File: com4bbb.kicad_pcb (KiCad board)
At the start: 4 copper layers, 54.6 x 86.4 mm, 67 parts, among them J101 RS485, J102 PWR, J103 DCF77, J104 PPS, J201 USB_B_Micro, J202 JTAG, P8 BeagleBone_Black_Header, P9 BeagleBone_Black_Header, SW101 Reset, SW102 PWR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

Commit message: Add PPS output
Signed-off-by: Benedikt Spranger <b.spranger@linutronix.de>
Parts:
- added J105: PPSOUT, Connector_PinHeader_2.54mm:PinHeader_1x02_P2.54mm_Vertical, F.Cu at (160.9, 108.1)
- added Q101: AO3400A, Package_TO_SOT_SMD:SOT-23, F.Cu at (159.9, 102.9)
- added R119: 100, Resistor_SMD:R_0402_1005Metric, F.Cu at (159.6, 99.4)
- added R120: 47k, Resistor_SMD:R_0402_1005Metric, F.Cu at (160.9, 99.4)
- added R121: 1k, Resistor_SMD:R_0402_1005Metric, F.Cu at (162.4, 102.6)
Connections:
- P9 pad 42: unconnected-(P9-Pin_42-Pad42) -> /PPS_OUT
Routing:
- net +5V: track 9.05 -> 75.3 mm, vias 0 -> 1
- net /PPS_OUT: track 0.00 -> 49.4 mm, vias 0 -> 2
- net Net-(J105-Pin_1): track 0.00 -> 7.00 mm
- net Net-(Q101-G): track 0.00 -> 3.32 mm

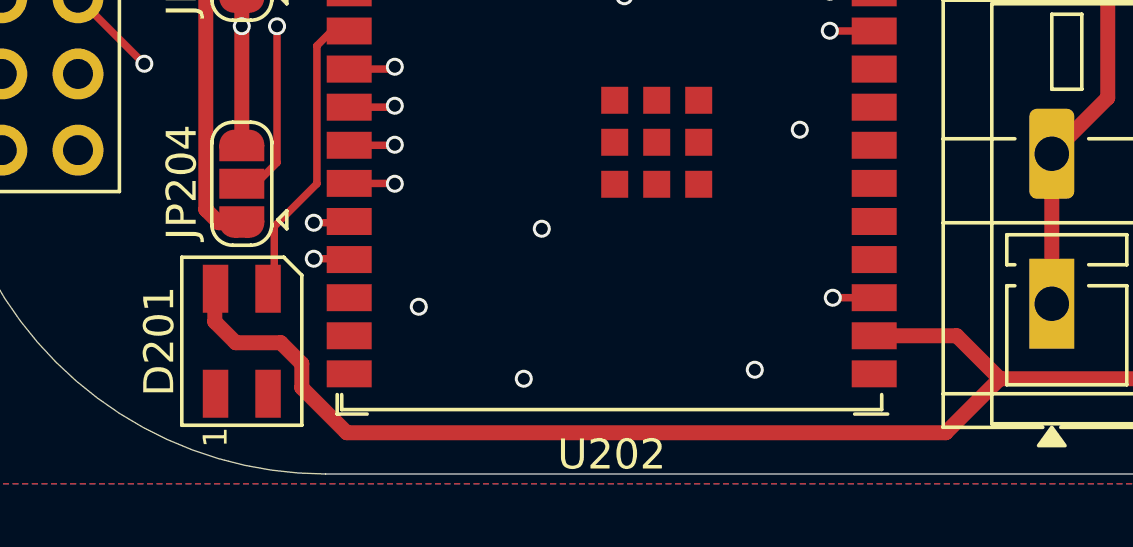
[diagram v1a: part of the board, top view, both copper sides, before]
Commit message: Fix SK6812 footprint mess
Signed-off-by: Benedikt Spranger <b.spranger@linutronix.de>
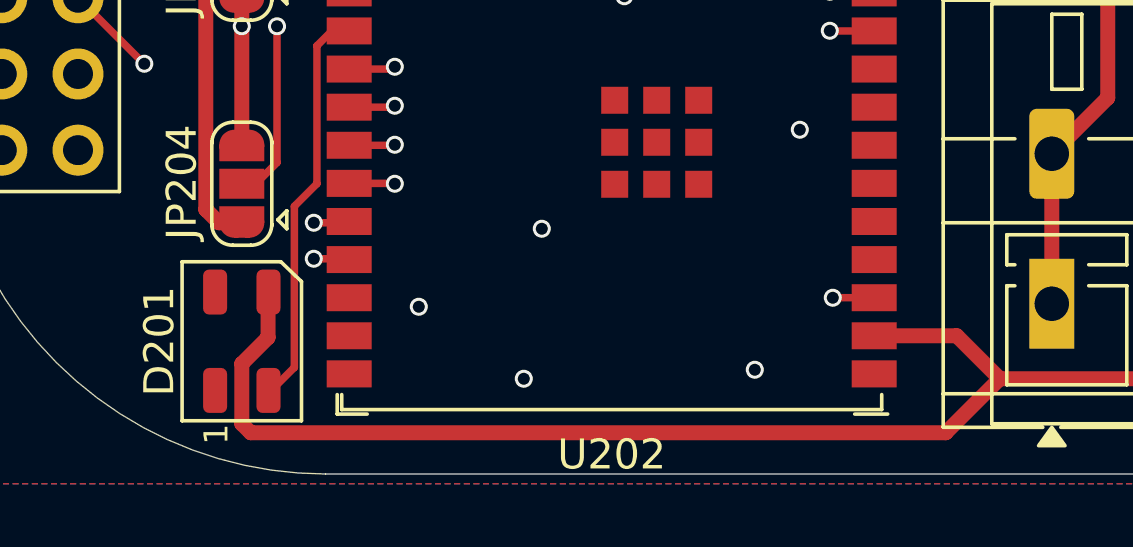
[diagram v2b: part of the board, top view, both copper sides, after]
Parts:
- D201: value SK6812MINI -> SK6812MINI-HS-012; footprint LED_SMD:LED_SK6812MINI_PLCC4_3.5x3.5mm_P1.75mm -> LED_SMD:LED_WS2812B-Mini_PLCC4_3.5x3.5mm
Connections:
- D201 pad 1: unconnected-(D201-DOUT-Pad1) -> GNDD
- D201 pad 2: GNDD -> Net-(D201-DIN)
- D201 pad 3: Net-(D201-DIN) -> +3V3
- D201 pad 4: +3V3 -> unconnected-(D201-DOUT-Pad4)
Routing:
- net Net-(D201-DIN): track 9.18 -> 13.0 mm
- net +3V3: track 222.5 -> 223.5 mm
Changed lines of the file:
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@@
 	(net 33 "Net-(D114-K)")
 	(net 34 "Net-(D114-A)")
-	(net 35 "unconnected-(D201-DOUT-Pad1)")
+	(net 35 "unconnected-(D201-DOUT-Pad4)")
 	(net 36 "Net-(D201-DIN)")
 	(net 37 "Net-(J201-Shield)")
@@
 		)
 	)
-	(footprint "LED_SMD:LED_SK6812MINI_PLCC4_3.5x3.5mm_P1.75mm"
+	(footprint "LED_SMD:LED_WS2812B-Mini_PLCC4_3.5x3.5mm"
 		(layer "F.Cu")
 		(at 124.3701 124.6324 90)
-		(descr "3.5mm x 3.5mm PLCC4 Addressable RGB LED NeoPixel, https://cdn-shop.adafruit.com/product-files/2686/SK6812MINI_REV.01-1-2.pdf")
-		(tags "LED RGB NeoPixel Mini PLCC-4 3535")
+		(descr "Addressable RGB LED NeoPixel Mini, 12 mA, https://web.archive.org/web/20200131233647/http://www.world-semi.com/DownLoadFile/112")
+		(tags "LED RGB NeoPixel Mini")
 		(property "Reference" "D201"
 			(at 0 -2.75 90)
@@
 			)
 		)
-		(property "Value" "SK6812MINI"
+		(property "Value" "SK6812MINI-HS-012"
 			(at 0 3.25 90)
 			(layer "F.Fab")
@@
 			)
 		)
-		(property "Datasheet" "https://cdn-shop.adafruit.com/product-files/2686/SK6812MINI_REV.01-1-2.pdf"
+		(property "Datasheet" "https://jlcpcb.com/api/file/downloadByFileSystemAccessId/8588920813789581312"
 			(at 0 0 90)
 			(unlocked yes)
@@
 			)
 		)
-		(property ki_fp_filters "LED*SK6812MINI*PLCC*3.5x3.5mm*P1.75mm*")
+		(property ki_fp_filters "LED*WS2812B-Mini*PLCC*3.5x3.5mm")
 		(sheetname "/ESP32/")
 		(sheetfile "esp32.kicad_sch")
 		(attr smd)
 		(fp_line
-			(start -2.8 -2)
-			(end 2.8 -2)
+			(start -2.65 -1.99)
+			(end 2.65 -1.99)
 			(stroke
 				(width 0.12)
@@
 		)
 		(fp_line
-			(start -2.8 -2)
-			(end -2.8 2)
+			(start -2.65 -1.99)
+			(end -2.65 1.99)
 			(stroke
 				(width 0.12)
@@
 		)
 		(fp_line
-			(start 2.8 1.4)
-			(end 2.8 -2)
+			(start 2.65 1.3)
+			(end 2.65 -1.99)
 			(stroke
 				(width 0.12)
@@
 		)
 		(fp_line
-			(start 2.8 1.4)
-			(end 2.2 2)
+			(start 2.65 1.3)
+			(end 1.99 1.99)
 			(stroke
 				(width 0.12)
@@
 		)
 		(fp_line
-			(start -2.8 2)
-			(end 2.2 2)
+			(start -2.65 1.99)
+			(end 1.99 1.99)
 			(stroke
 				(width 0.12)
@@
 		)
 		(fp_line
-			(start 2.8 -2)
-			(end -2.8 -2)
+			(start 2.64 -1.98)
+			(end -2.64 -1.98)
 			(stroke
 				(width 0.05)
@@
 		)
 		(fp_line
-			(start -2.8 -2)
-			(end -2.8 2)
+			(start -2.64 -1.98)
+			(end -2.64 1.98)
 			(stroke
 				(width 0.05)
@@
 		)
 		(fp_line
-			(start 2.8 2)
-			(end 2.8 -2)
+			(start 2.64 1.98)
+			(end 2.64 -1.98)
 			(stroke
 				(width 0.05)
@@
 		)
 		(fp_line
-			(start -2.8 2)
-			(end 2.8 2)
+			(start -2.64 1.98)
+			(end 2.64 1.98)
 			(stroke
 				(width 0.05)
@@
 		)
 		(fp_line
-			(start 1.75 -1.75)
-			(end -1.75 -1.75)
+			(start 1.73 -1.73)
+			(end -1.73 -1.73)
 			(stroke
 				(width 0.1)
@@
 		)
 		(fp_line
-			(start -1.75 -1.75)
-			(end -1.75 1.75)
+			(start -1.73 -1.73)
+			(end -1.73 1.73)
 			(stroke
 				(width 0.1)
@@
 		)
 		(fp_line
-			(start 1.75 0.75)
-			(end 0.75 1.75)
+			(start 1.73 0.86)
+			(end 0.86 1.73)
 			(stroke
 				(width 0.1)
@@
 		)
 		(fp_line
-			(start 1.75 1.75)
-			(end 1.75 -1.75)
+			(start 1.73 1.73)
+			(end 1.73 -1.73)
 			(stroke
 				(width 0.1)
@@
 		)
 		(fp_line
-			(start -1.75 1.75)
-			(end 1.75 1.75)
+			(start -1.73 1.73)
+			(end 1.73 1.73)
 			(stroke
 				(width 0.1)
@@
 		(fp_circle
 			(center 0 0)
-			(end 0 -1.5)
+			(end 1.1 0)
 			(stroke
 				(width 0.1)
@@
 		)
 		(fp_text user "1"
-			(at -3.2 -0.875 90)
+			(at -3.1 -0.85 90)
 			(unlocked yes)
 			(layer "F.SilkS")
@@
 			(effects
 				(font
-					(size 0.5 0.5)
-					(thickness 0.1)
+					(size 0.8 0.8)
+					(thickness 0.15)
 				)
 			)
 		)
-		(pad "1" smd rect
-			(at -1.75 -0.875 90)
-			(size 1.6 0.85)
-			(layers "F.Cu" "F.Mask" "F.Paste")
-			(net 35 "unconnected-(D201-DOUT-Pad1)")
-			(pinfunction "DOUT")
-			(pintype "output+no_connect")
-		)
-		(pad "2" smd rect
-			(at -1.75 0.875 90)
-			(size 1.6 0.85)
+		(pad "1" smd roundrect
+			(at -1.64 -0.89 90)
+			(size 1.5 0.8)
 			(layers "F.Cu" "F.Mask" "F.Paste")
+			(roundrect_rratio 0.25)
 			(net 1 "GNDD")
 			(pinfunction "VSS")
 			(pintype "power_in")
 		)
-		(pad "3" smd rect
-			(at 1.75 0.875 90)
-			(size 1.6 0.85)
+		(pad "2" smd roundrect
+			(at -1.64 0.89 90)
+			(size 1.5 0.8)
 			(layers "F.Cu" "F.Mask" "F.Paste")
+			(roundrect_rratio 0.25)
 			(net 36 "Net-(D201-DIN)")
 			(pinfunction "DIN")
 			(pintype "input")
 		)
-		(pad "4" smd rect
-			(at 1.75 -0.875 90)
-			(size 1.6 0.85)
+		(pad "3" smd roundrect
+			(at 1.64 0.89 90)
+			(size 1.5 0.8)
 			(layers "F.Cu" "F.Mask" "F.Paste")
+			(roundrect_rratio 0.25)
 			(net 2 "+3V3")
 			(pinfunction "VDD")
 			(pintype "power_in")
 		)
+		(pad "4" smd roundrect
+			(at 1.64 -0.89 90)
+			(size 1.5 0.8)
+			(layers "F.Cu" "F.Mask" "F.Paste")
+			(roundrect_rratio 0.25)
+			(net 35 "unconnected-(D201-DOUT-Pad4)")
+			(pinfunction "DOUT")
+			(pintype "output+no_connect")
+		)
 		(embedded_fonts no)
-		(model "${KICAD9_3DMODEL_DIR}/LED_SMD.3dshapes/LED_SK6812MINI_PLCC4_3.5x3.5mm_P1.75mm.step"
+		(model "${KICAD9_3DMODEL_DIR}/LED_SMD.3dshapes/LED_WS2812B-Mini_PLCC4_3.5x3.5mm.step"
 			(offset
 				(xyz 0 0 0)
@@
 	)
 	(segment
+		(start 125.2451 124.5074)
+		(end 125.2451 122.8824)
+		(width 0.5)
+		(layer "F.Cu")
+		(net 2)
+	)
+	(segment
 		(start 133.8801 87.1324)
 		(end 133.8801 89.2824)
@@
 	)
 	(segment
+		(start 124.6701 127.6824)
+		(end 124.3701 127.3824)
+		(width 0.5)
+		(layer "F.Cu")
+		(net 2)
+	)
+	(segment
 		(start 135.4511 91.920674)
 		(end 135.4511 90.8534)
@@
 	)
 	(segment
-		(start 126.3701 125.3804)
-		(end 125.6721 124.6824)
-		(width 0.5)
-		(layer "F.Cu")
-		(net 2)
-	)
-	(segment
-		(start 126.3701 126.1824)
-		(end 126.3701 125.3804)
-		(width 0.5)
-		(layer "F.Cu")
-		(net 2)
-	)
-	(segment
 		(start 151.4201 75.3824)
 		(end 151.3701 75.3324)
@@
 	)
 	(segment
-		(start 133.8801 86.3124)
-		(end 133.8801 87.1324)
+		(start 124.3701 125.3824)
+		(end 125.2451 124.5074)
+		(width 0.5)
+		(layer "F.Cu")
+		(net 2)
+	)
+	(segment
+		(start 149.6349 125.8824)
+		(end 147.8349 127.6824)
 		(width 0.5)
 		(layer "F.Cu")
@@
 	)
 	(segment
-		(start 125.6721 124.6824)
-		(end 124.1701 124.6824)
+		(start 133.8801 86.3124)
+		(end 133.8801 87.1324)
 		(width 0.5)
 		(layer "F.Cu")
@@
 	)
 	(segment
+		(start 147.8349 127.6824)
+		(end 124.6701 127.6824)
+		(width 0.5)
+		(layer "F.Cu")
+		(net 2)
+	)
+	(segment
 		(start 158.6 110.9323)
 		(end 158.6 125.0525)
@@
 	)
 	(segment
+		(start 124.3701 127.3824)
+		(end 124.3701 125.3824)
+		(width 0.5)
+		(layer "F.Cu")
+		(net 2)
+	)
+	(segment
 		(start 156.52511 101.07491)
 		(end 156.52511 104.5)
@@
 	)
 	(segment
-		(start 147.8349 127.6824)
-		(end 127.8701 127.6824)
-		(width 0.5)
-		(layer "F.Cu")
-		(net 2)
-	)
-	(segment
 		(start 155.7751 105.25001)
 		(end 156.52511 104.5)
@@
 	)
 	(segment
-		(start 149.6349 125.8824)
-		(end 147.8349 127.6824)
-		(width 0.5)
-		(layer "F.Cu")
-		(net 2)
-	)
-	(segment
 		(start 155.7751 108.1074)
 		(end 158.6 110.9323)
@@
 	)
 	(segment
-		(start 123.4701 123.9824)
-		(end 124.1701 124.6824)
-		(width 0.5)
-		(layer "F.Cu")
-		(net 2)
-	)
-	(segment
 		(start 116.3701 64.9224)
 		(end 118.9101 64.9224)
@@
 	)
 	(segment
-		(start 123.4701 122.9074)
-		(end 123.4701 123.9824)
-		(width 0.5)
-		(layer "F.Cu")
-		(net 2)
-	)
-	(segment
-		(start 127.8701 127.6824)
-		(end 126.3701 126.1824)
-		(width 0.5)
-		(layer "F.Cu")
-		(net 2)
-	)
-	(segment
 		(start 135.4511 90.8534)
 		(end 133.8801 89.2824)
@@
 	)
 	(segment
+		(start 126.12205 120.13435)
+		(end 126.12205 125.50545)
+		(width 0.25)
+		(layer "F.Cu")
+		(net 36)
+	)
+	(segment
 		(start 126.874 119.3824)
 		(end 126.874 114.784)
@@
 	)
 	(segment
-		(start 125.4511 120.8053)
-		(end 126.874 119.3824)
+		(start 126.12205 125.50545)
+		(end 125.2451 126.3824)
 		(width 0.25)
 		(layer "F.Cu")
@@
 	)
 	(segment
-		(start 126.874 114.784)
-		(end 127.368 114.29)
+		(start 126.12205 120.13435)
+		(end 126.874 119.3824)
 		(width 0.25)
 		(layer "F.Cu")
@@
 	)
 	(segment
-		(start 125.4511 122.6764)
-		(end 125.4511 120.8053)
+		(start 126.874 114.784)
+		(end 127.368 114.29)
 		(width 0.25)
 		(layer "F.Cu")
